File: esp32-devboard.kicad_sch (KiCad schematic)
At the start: 0 parts

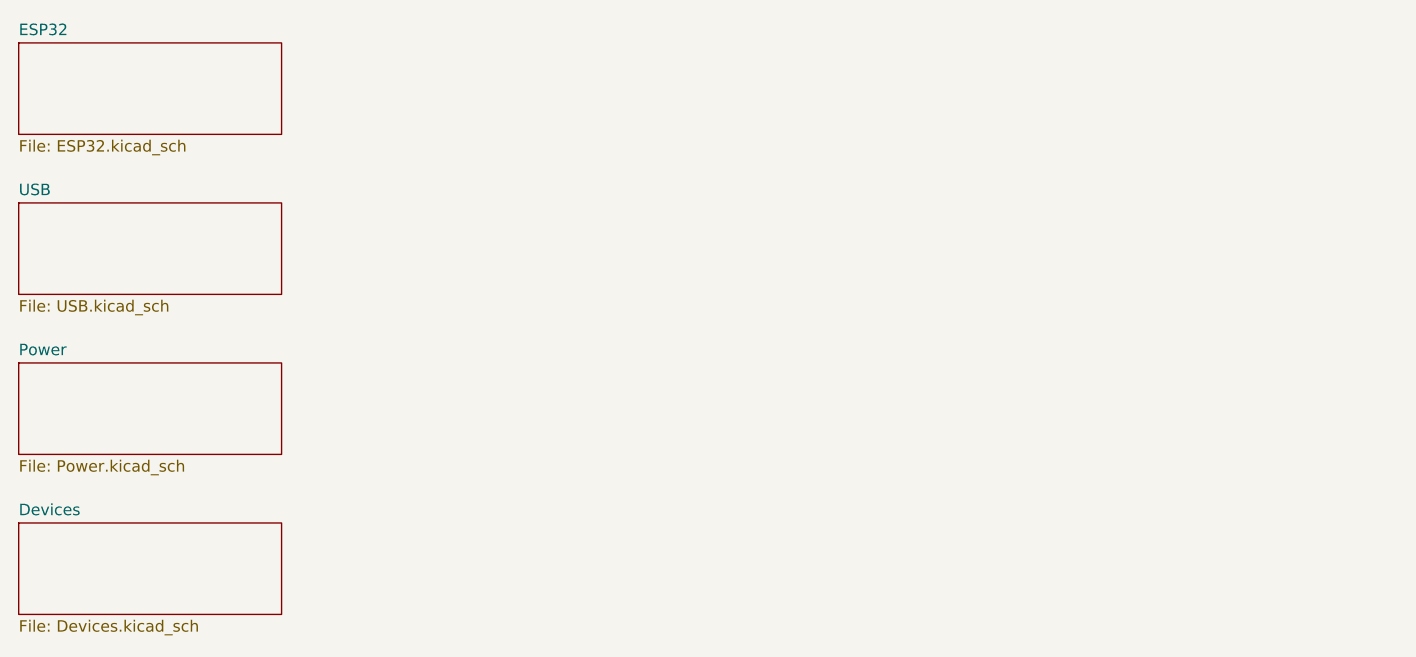
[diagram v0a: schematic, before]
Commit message: added USB-C connector
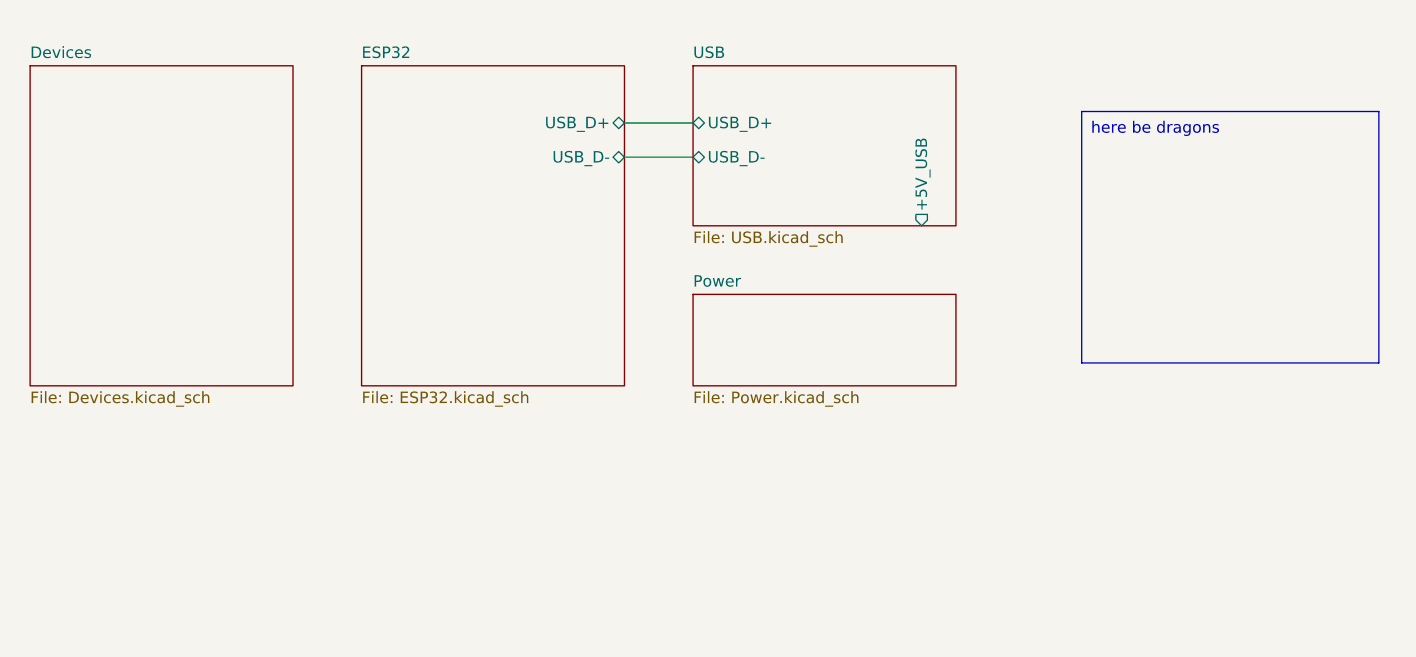
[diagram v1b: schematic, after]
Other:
- sheet ESP32 ports: added USB_D+, USB_D-; removed none
- sheet USB ports: added +5V_USB, USB_D+, USB_D-; removed none
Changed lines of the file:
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@@
 		(rev "v1.0")
 	)
-	(sheet
-		(at 21.59 22.86)
-		(size 29.21 10.16)
+	(wire
+		(pts
+			(xy 88.9 35.56) (xy 96.52 35.56)
+		)
+		(stroke
+			(width 0)
+			(type default)
+		)
+	)
+	(wire
+		(pts
+			(xy 88.9 31.75) (xy 96.52 31.75)
+		)
+		(stroke
+			(width 0)
+			(type default)
+		)
+	)
+	(text_box "here be dragons"
+		(exclude_from_sim no)
+		(at 139.7 30.48 0)
+		(size 33.02 27.94)
+		(stroke
+			(width 0)
+			(type default)
+		)
+		(fill
+			(type none)
+		)
+		(effects
+			(font
+				(size 1.27 1.27)
+			)
+			(justify left top)
+		)
+	)
+	(sheet
+		(at 59.69 25.4)
+		(size 29.21 35.56)
 		(fields_autoplaced yes)
 		(stroke
@@
 		)
 		(property "Sheetname" "ESP32"
-			(at 21.59 22.1484 0)
+			(at 59.69 24.6884 0)
 			(effects
 				(font
@@
 		)
 		(property "Sheetfile" "ESP32.kicad_sch"
-			(at 21.59 33.6046 0)
+			(at 59.69 61.5446 0)
 			(effects
 				(font
@@
 				)
 				(justify left top)
+			)
+		)
+		(pin "USB_D+" bidirectional
+			(at 88.9 31.75 0)
+			(effects
+				(font
+					(size 1.27 1.27)
+				)
+				(justify right)
+			)
+		)
+		(pin "USB_D-" bidirectional
+			(at 88.9 35.56 0)
+			(effects
+				(font
+					(size 1.27 1.27)
+				)
+				(justify right)
 			)
 		)
@@
 	)
 	(sheet
-		(at 21.59 40.64)
-		(size 29.21 10.16)
+		(at 96.52 25.4)
+		(size 29.21 17.78)
 		(fields_autoplaced yes)
 		(stroke
@@
 		)
 		(property "Sheetname" "USB"
-			(at 21.59 39.9284 0)
+			(at 96.52 24.6884 0)
 			(effects
 				(font
@@
 		)
 		(property "Sheetfile" "USB.kicad_sch"
-			(at 21.59 51.3846 0)
+			(at 96.52 43.7646 0)
 			(effects
 				(font
@@
 				)
 				(justify left top)
+			)
+		)
+		(pin "+5V_USB" output
+			(at 121.92 43.18 270)
+			(effects
+				(font
+					(size 1.27 1.27)
+				)
+				(justify left)
+			)
+		)
+		(pin "USB_D-" bidirectional
+			(at 96.52 35.56 180)
+			(effects
+				(font
+					(size 1.27 1.27)
+				)
+				(justify left)
+			)
+		)
+		(pin "USB_D+" bidirectional
+			(at 96.52 31.75 180)
+			(effects
+				(font
+					(size 1.27 1.27)
+				)
+				(justify left)
 			)
 		)
@@
 	)
 	(sheet
-		(at 21.59 58.42)
+		(at 96.52 50.8)
 		(size 29.21 10.16)
 		(fields_autoplaced yes)
@@
 		)
 		(property "Sheetname" "Power"
-			(at 21.59 57.7084 0)
+			(at 96.52 50.0884 0)
 			(effects
 				(font
@@
 		)
 		(property "Sheetfile" "Power.kicad_sch"
-			(at 21.59 69.1646 0)
+			(at 96.52 61.5446 0)
 			(effects
 				(font
@@
 	)
 	(sheet
-		(at 21.59 76.2)
-		(size 29.21 10.16)
+		(at 22.86 25.4)
+		(size 29.21 35.56)
 		(fields_autoplaced yes)
 		(stroke
@@
 		)
 		(property "Sheetname" "Devices"
-			(at 21.59 75.4884 0)
+			(at 22.86 24.6884 0)
 			(effects
 				(font
@@
 		)
 		(property "Sheetfile" "Devices.kicad_sch"
-			(at 21.59 86.9446 0)
-			(effects
-				(font
+			(at 22.86 61.5446 0)
+			(effects
+				(font

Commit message: USB and PWR sch
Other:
- sheet Power ports: added +3.3v, +5V; removed none
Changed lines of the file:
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@@
+	(wire
+		(pts
+			(xy 121.92 43.18) (xy 121.92 50.8)
+		)
+		(stroke
+			(width 0)
+			(type default)
+		)
+	)
+	(wire
+		(pts
+			(xy 125.73 58.42) (xy 130.81 58.42)
+		)
+		(stroke
+			(width 0)
+			(type default)
+		)
+	)
+	(wire
+		(pts
+			(xy 130.81 58.42) (xy 130.81 53.34)
+		)
+		(stroke
+			(width 0)
+			(type default)
+		)
+	)
 	(wire
 		(pts
@@
 		)
 	)
+	(symbol
+		(lib_id "power:+3.3V")
+		(at 130.81 53.34 0)
+		(unit 1)
+		(exclude_from_sim no)
+		(in_bom yes)
+		(on_board yes)
+		(dnp no)
+		(fields_autoplaced yes)
+		(property "Reference" "#PWR013"
+			(at 130.81 57.15 0)
+			(effects
+				(font
+					(size 1.27 1.27)
+				)
+				(hide yes)
+			)
+		)
+		(property "Value" "+3.3V"
+			(at 130.81 48.26 0)
+			(effects
+				(font
+					(size 1.27 1.27)
+				)
+			)
+		)
+		(property "Footprint" ""
+			(at 130.81 53.34 0)
+			(effects
+				(font
+					(size 1.27 1.27)
+				)
+				(hide yes)
+			)
+		)
+		(property "Datasheet" ""
+			(at 130.81 53.34 0)
+			(effects
+				(font
+					(size 1.27 1.27)
+				)
+				(hide yes)
+			)
+		)
+		(property "Description" "Power symbol creates a global label with name \"+3.3V\""
+			(at 130.81 53.34 0)
+			(effects
+				(font
+					(size 1.27 1.27)
+				)
+				(hide yes)
+			)
+		)
+		(pin "1"
+		)
+		(instances
+			(project ""
+				(path "/0204cec0-d71e-48a7-8736-ccb0d3e9b02c"
+					(reference "#PWR013")
+					(unit 1)
+				)
+			)
+		)
+	)
 	(sheet
 		(at 59.69 25.4)
@@
 			)
 		)
+		(pin "+3.3v" output
+			(at 125.73 58.42 0)
+			(effects
+				(font
+					(size 1.27 1.27)
+				)
+				(justify right)
+			)
+		)
+		(pin "+5V" input
+			(at 121.92 50.8 90)
+			(effects
+				(font
+					(size 1.27 1.27)
+				)
+				(justify right)
+			)
+		)

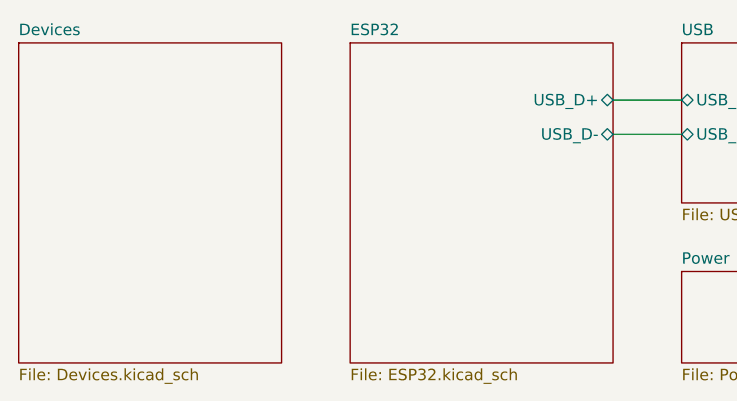
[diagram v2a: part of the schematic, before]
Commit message: add BOOT/RST switches
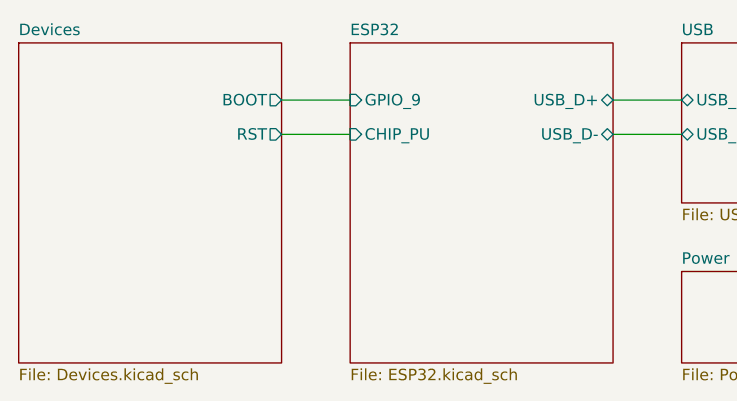
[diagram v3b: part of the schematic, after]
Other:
- sheet Devices ports: added BOOT, RST; removed none
- sheet ESP32 ports: added CHIP_PU, GPIO_9; removed none
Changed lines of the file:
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@@
+	(wire
+		(pts
+			(xy 52.07 35.56) (xy 59.69 35.56)
+		)
+		(stroke
+			(width 0)
+			(type default)
+		)
+	)
 	(wire
 		(pts
@@
 		(pts
 			(xy 88.9 31.75) (xy 96.52 31.75)
+		)
+		(stroke
+			(width 0)
+			(type default)
+		)
+	)
+	(wire
+		(pts
+			(xy 52.07 31.75) (xy 59.69 31.75)
 		)
 		(stroke
@@
 			)
 		)
+		(pin "CHIP_PU" input
+			(at 59.69 35.56 180)
+			(effects
+				(font
+					(size 1.27 1.27)
+				)
+				(justify left)
+			)
+		)
+		(pin "GPIO_9" input
+			(at 59.69 31.75 180)
+			(effects
+				(font
+					(size 1.27 1.27)
+				)
+				(justify left)
+			)
+		)
 		(instances
 			(project "esp32-devboard"
@@
 			)
 		)
+		(pin "BOOT" output
+			(at 52.07 31.75 0)
+			(effects
+				(font
+					(size 1.27 1.27)
+				)
+				(justify right)
+			)
+		)
+		(pin "RST" output
+			(at 52.07 35.56 0)
+			(effects
+				(font
+					(size 1.27 1.27)
+				)
+				(justify right)
+			)
+		)

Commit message: finished sch? (need P/Ns)
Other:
- sheet Devices ports: added FLIP, FLOP, LED_0; removed none
- sheet ESP32 ports: added GPIO_14, GPIO_15, GPIO_18; removed none
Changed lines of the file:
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@@
+	(wire
+		(pts
+			(xy 52.07 43.18) (xy 59.69 43.18)
+		)
+		(stroke
+			(width 0)
+			(type default)
+		)
+	)
 	(wire
 		(pts
@@
 	(wire
 		(pts
+			(xy 52.07 39.37) (xy 59.69 39.37)
+		)
+		(stroke
+			(width 0)
+			(type default)
+		)
+	)
+	(wire
+		(pts
 			(xy 130.81 58.42) (xy 130.81 53.34)
 		)
@@
 		)
 	)
-	(text_box "here be dragons"
+	(wire
+		(pts
+			(xy 52.07 46.99) (xy 59.69 46.99)
+		)
+		(stroke
+			(width 0)
+			(type default)
+		)
+	)
+	(text_box "here be dragons (board notes at some point)"
 		(exclude_from_sim no)
 		(at 139.7 30.48 0)
@@
 			)
 		)
+		(pin "GPIO_14" input
+			(at 59.69 39.37 180)
+			(effects
+				(font
+					(size 1.27 1.27)
+				)
+				(justify left)
+			)
+		)
+		(pin "GPIO_15" input
+			(at 59.69 43.18 180)
+			(effects
+				(font
+					(size 1.27 1.27)
+				)
+				(justify left)
+			)
+		)
+		(pin "GPIO_18" output
+			(at 59.69 46.99 180)
+			(effects
+				(font
+					(size 1.27 1.27)
+				)
+				(justify left)
+			)
+		)
 		(instances
 			(project "esp32-devboard"
@@
 			(effects
 				(font
+					(size 1.27 1.27)
+				)
+				(justify right)
+			)
+		)
+		(pin "FLIP" output
+			(at 52.07 39.37 0)
+			(effects
+				(font
+					(size 1.27 1.27)
+				)
+				(justify right)
+			)
+		)
+		(pin "FLOP" output
+			(at 52.07 43.18 0)
+			(effects
+				(font
+					(size 1.27 1.27)
+				)
+				(justify right)
+			)
+		)
+		(pin "LED_0" input
+			(at 52.07 46.99 0)
+			(effects
+				(font
